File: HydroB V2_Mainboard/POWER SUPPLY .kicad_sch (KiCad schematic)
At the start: 6 parts, among them U2 TPS7A2633DRVR

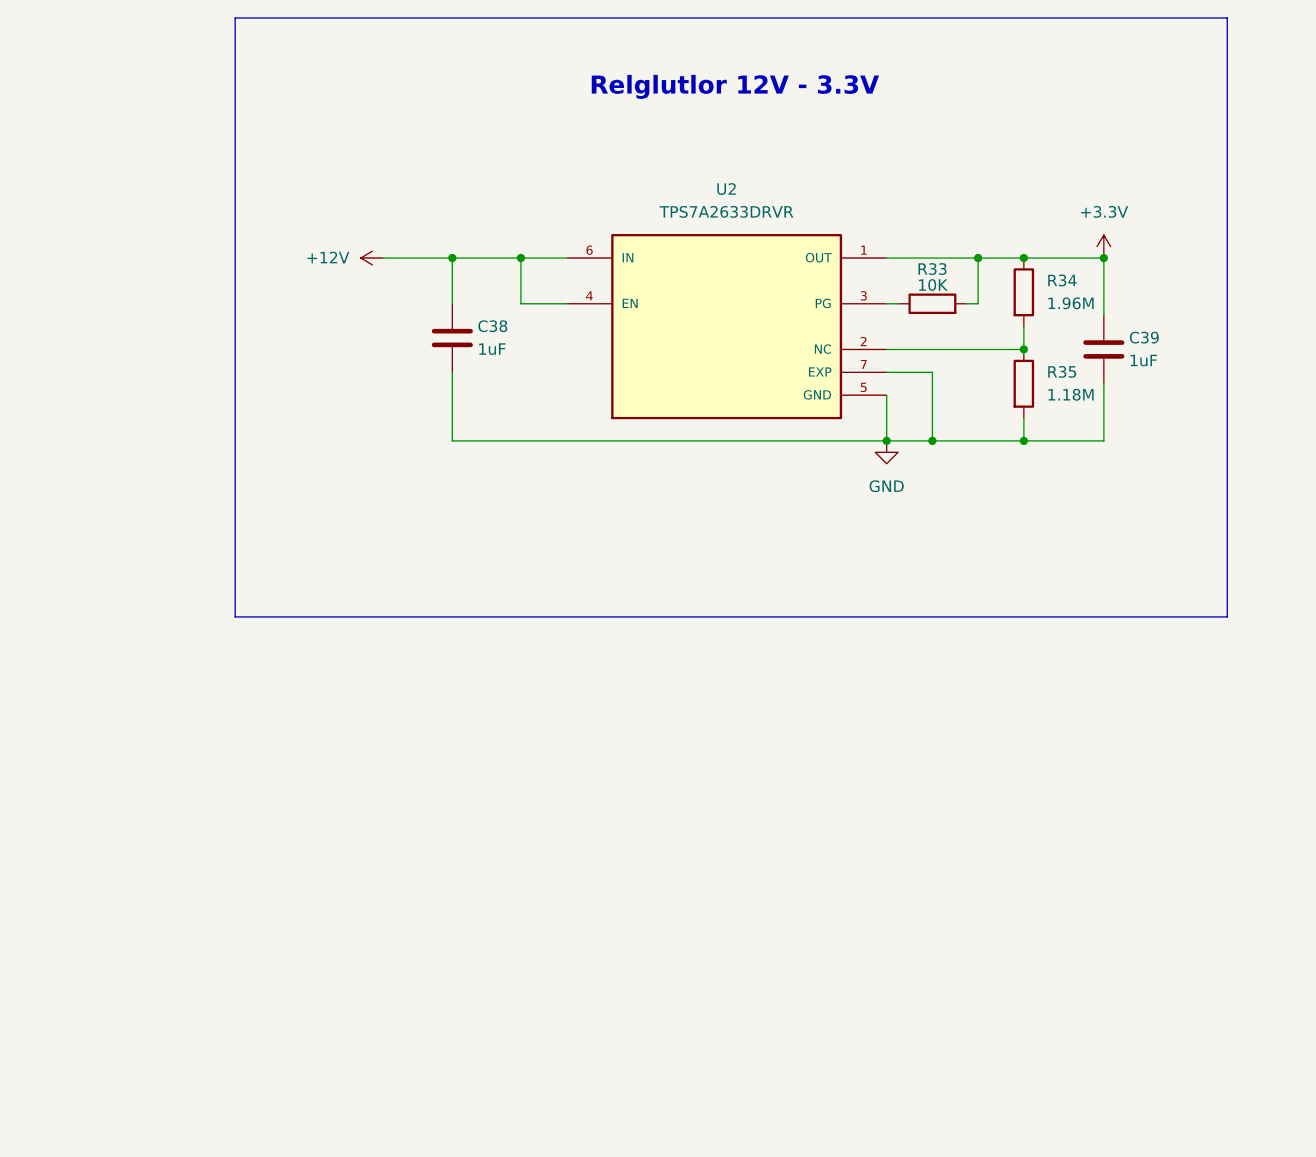
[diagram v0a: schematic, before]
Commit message: Update LCD schematic
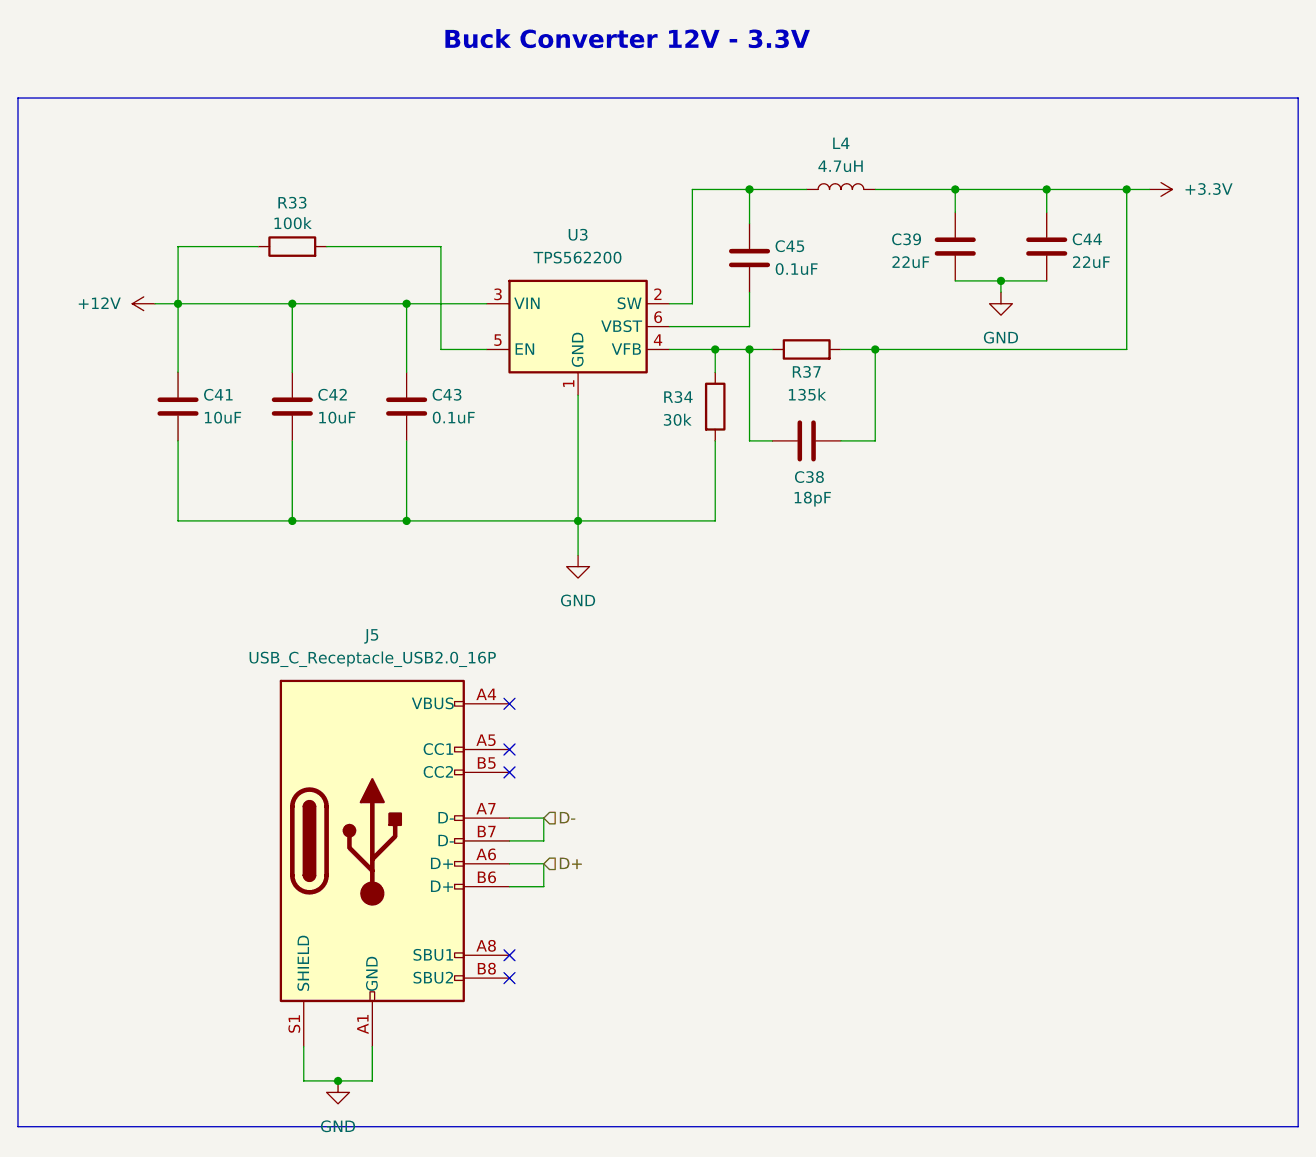
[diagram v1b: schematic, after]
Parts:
- removed R35: 1.18M, Resistor_SMD:R_0603_1608Metric, symbol Device:R
- removed U2: TPS7A2633DRVR, TPS7A2633DRVR:SON65P200X200X80-7N, symbol TPS7A2633DRVR:TPS7A2633DRVR
- added C41, C42: 10uF, Capacitor_SMD:C_0603_1608Metric, symbol Device:C
- added C43, C45: 0.1uF, Capacitor_SMD:C_0603_1608Metric, symbol Device:C
- added C44: 22uF, Capacitor_SMD:C_0603_1608Metric, symbol Device:C
- added J5: USB_C_Receptacle_USB2.0_16P, symbol Connector:USB_C_Receptacle_USB2.0_16P
- added L4: 4.7uH, symbol Device:L
- added R37: 135k, Resistor_SMD:R_0603_1608Metric, symbol Device:R
- added U3: TPS562200, Package_TO_SOT_SMD:SOT-23-6, symbol Regulator_Switching:TPS562200
- C38: value 1uF -> 18pF
- C39: value 1uF -> 22uF
- R33: value 10K -> 100k
- R34: value 1.96M -> 30k
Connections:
- net +12V: now also R33.1, C41.1, C42.1, C43.1, U3.3 (VIN); no longer C38.1
- net +3.3V: now also C38.2, C44.1, L4.2, R37.2; no longer R33.2, R34.1
- net GND: now also R34.2, C41.2, C42.2, C43.2, C44.2, J5.A1 (GND), J5.A12 (GND), J5.B1 (GND), J5.B12 (GND), J5.S1 (SHIELD), U3.1 (GND); no longer C38.2
- new net: C45.1, L4.1, U3.2 (SW)
- new net: C45.2, U3.6 (VBST)
- new net: C38.1, R34.1, R37.1, U3.4 (VFB)
- new net: R33.2, U3.5 (EN)
- new net: J5.A4 (VBUS), J5.A9 (VBUS), J5.B4 (VBUS), J5.B9 (VBUS)
- new net D+: J5.A6 (D+), J5.B6 (D+)
- new net D-: J5.A7 (D-), J5.B7 (D-)
- no-connect marks 0 -> 5
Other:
- note added: "Buck Converter 12V - 3.3V"
- note removed: "Relglutlor 12V - 3.3V"
- moved on the sheet: C38, C39, R33, R34

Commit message: Schematic mainboard update
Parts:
- added C10: 0.1uF, Capacitor_SMD:C_0603_1608Metric, symbol Device:C_Small
- added C11, C12: 22uF, Capacitor_SMD:C_0603_1608Metric, symbol Device:C_Small
- added C7: 10uF, Capacitor_SMD:CP_Elec_4x3, symbol Device:C
- added C8: 0.1uF, Capacitor_SMD:C_0603_1608Metric, symbol Device:C
- added C9: 75pF, Capacitor_SMD:C_0603_1608Metric, symbol Device:C_Small
- added J1: Conn_01x02_Pin, Connector_Phoenix_MC:PhoenixContact_MCV_1,5_2-G-3.81_1x02_P3.81mm_Vertical, symbol Connector:Conn_01x02_Pin
- added L1: 15uH, Inductor_SMD:L_Vishay_IHLP-2020, symbol Device:L
- added PS1: HLK-20M12, Converter_ACDC:Converter_ACDC_Hi-Link_HLK-20Mxx, symbol Converter_ACDC:HLK-20M12
- added R12: 100K, Resistor_SMD:R_0603_1608Metric, symbol Device:R
- added R13: 13.3K, Resistor_SMD:R_0603_1608Metric, symbol Device:R
- added R14: 49.9, Resistor_SMD:R_0603_1608Metric, symbol Device:R
- added R5: 1k, Resistor_SMD:R_0402_1005Metric, symbol Device:R
- added U4: TPS54202DDC, Package_TO_SOT_SMD:SOT-23-6, symbol Regulator_Switching:TPS54202DDC
- C41: footprint Capacitor_SMD:C_0603_1608Metric -> Capacitor_SMD:CP_Elec_4x3
- J5: footprint (none) -> Connector_USB:USB_C_Receptacle_G-Switch_GT-USB-7010ASV
- L4: footprint (none) -> Inductor_SMD:L_Bourns_SRP5030T
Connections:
- net +12V: now also C7.1, C8.1, PS1.4 (+Vout), U4.3 (VIN)
- net GND: now also C11.2, C12.2, C7.2, C8.2, PS1.3 (-Vout), R13.2, U4.1 (GND)
- net +5V: now reaches J5.A4 (VBUS), J5.A9 (VBUS), J5.B4 (VBUS), J5.B9 (VBUS)
- net +5V: now also C11.1, C12.1, L1.2, R14.2
- net A5: now reaches J5.A5 (CC1)
- new net: C9.2, R12.2, R13.1, U4.4 (FB)
- new net: C9.1, R12.1, R14.1
- new net: R5.1, U4.5 (EN)
- new net: C10.2, L1.1, U4.2 (SW)
- new net: C10.1, U4.6 (BOOT)
- new net En: R5.2
- new net L: J1.2 (Pin_2), PS1.1 (AC/L)
- new net N: J1.1 (Pin_1), PS1.2 (AC/N)
- no-connect marks 5 -> 3
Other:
- note added: "AC/DC input 220V-12V"
- note added: "Buck Converter 12V - 5V - 3.3V"
- note added: "Type C"
- note removed: "Buck Converter 12V - 3.3V"
- moved on the sheet: C38, C39, C41, C42, C43, C44, C45, J5, L4, R33, R34, R37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

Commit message: Mainboard schematic update
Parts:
- removed C10: 0.1uF, Capacitor_SMD:C_0603_1608Metric, symbol Device:C_Small
- removed C11, C12: 22uF, Capacitor_SMD:C_0603_1608Metric, symbol Device:C_Small
- removed C38: 18pF, Capacitor_SMD:C_0603_1608Metric, symbol Device:C
- removed C39, C44: 22uF, Capacitor_SMD:C_0603_1608Metric, symbol Device:C
- removed C41: 10uF, Capacitor_SMD:CP_Elec_4x3, symbol Device:C
- removed C42: 10uF, Capacitor_SMD:C_0603_1608Metric, symbol Device:C
- removed C43, C45: 0.1uF, Capacitor_SMD:C_0603_1608Metric, symbol Device:C
- removed C9: 75pF, Capacitor_SMD:C_0603_1608Metric, symbol Device:C_Small
- removed J1: Conn_01x02_Pin, Connector_Phoenix_MC:PhoenixContact_MCV_1,5_2-G-3.81_1x02_P3.81mm_Vertical, symbol Connector:Conn_01x02_Pin
- removed L4: 4.7uH, Inductor_SMD:L_Bourns_SRP5030T, symbol Device:L
- removed PS1: HLK-20M12, Converter_ACDC:Converter_ACDC_Hi-Link_HLK-20Mxx, symbol Converter_ACDC:HLK-20M12
- removed R33: 100k, Resistor_SMD:R_0603_1608Metric, symbol Device:R
- removed R34: 30k, Resistor_SMD:R_0603_1608Metric, symbol Device:R
- removed R37: 135k, Resistor_SMD:R_0603_1608Metric, symbol Device:R
- removed U3: TPS562200, Package_TO_SOT_SMD:SOT-23-6, symbol Regulator_Switching:TPS562200
- removed U4: TPS54202DDC, Package_TO_SOT_SMD:SOT-23-6, symbol Regulator_Switching:TPS54202DDC
- added C10, C11, C12, C13: 22uF, Capacitor_SMD:C_0805_2012Metric, symbol Device:C
- added C14, C15: 1uF, Capacitor_SMD:C_0805_2012Metric, symbol Device:C
- added C4: 10uF, Capacitor_SMD:CP_Elec_4x3, symbol Device:C
- added C6: 220nF, Capacitor_SMD:C_0805_2012Metric, symbol Device:C
- added C9: c, Capacitor_SMD:C_0805_2012Metric, symbol Device:C
- added D2: LED, LED_SMD:LED_0603_1608Metric_Pad1.05x0.95mm_HandSolder, symbol Device:LED
- added J6: 12V, DC Conn:DC conn, symbol Connector:Screw_Terminal_01x02
- added J7: Conn_01x02_Pin, Connector_PinHeader_2.00mm:PinHeader_1x02_P2.00mm_Vertical, symbol Connector:Conn_01x02_Pin
- added R15: 1.96M, Resistor_SMD:R_0402_1005Metric, symbol Device:R
- added R16: 1.18M, Resistor_SMD:R_0402_1005Metric, symbol Device:R
- added R17: 1k, Resistor_SMD:R_0603_1608Metric, symbol Device:R
- added U3: LMR33620ADDA, Package_SO:Texas_HSOP-8-1EP_3.9x4.9mm_P1.27mm_ThermalVias, symbol Regulator_Switching:LMR33620ADDA
- added U4: TPS7A2633DRVR, TPS7A2633DRVR:SON65P200X200X80-7N, symbol TPS7A2633DRVR:TPS7A2633DRVR
- C7: value 10uF -> 1uF; footprint Capacitor_SMD:CP_Elec_4x3 -> Capacitor_SMD:C_0805_2012Metric
- C8: value 0.1uF -> 100NF
- L1: value 15uH -> 10uH; footprint Inductor_SMD:L_Vishay_IHLP-2020 -> Inductor_SMD:L_Bourns_SRP5030T
- R12: value 100K -> 100k
- R13: value 13.3K -> 43.2k
- R14: value 49.9 -> 10K
- R5: value 1k -> 100k; footprint Resistor_SMD:R_0402_1005Metric -> Resistor_SMD:R_0603_1608Metric
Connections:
- net +12V: now also C4.1, C6.1, J6.1 (Pin_1), U3.2 (VIN), U3.3 (EN); no longer C7.1, C8.1
- net +3.3V: now also R14.2, C15.1, D2.2 (A), J7.1 (Pin_1), R15.1, U4.1 (OUT)
- net +5V: now also C14.1, U4.4 (EN), U4.6 (IN); no longer L1.2, R14.2
- net GND: now also R13.1, C10.2, C11.2, C12.2, C13.2, C14.2, C15.2, C4.2, C6.2, J6.2 (Pin_2), R16.2, R17.2, U3.1 (GND), U3.9 (GND), U4.5 (GND), U4.7 (EXP); no longer C8.2, R13.2
- net SW_OUT: now reaches R12.2
- net SW_OUT: now also L1.2, C10.1, C11.1, C12.1, C13.1, C9.1, J7.2 (Pin_2); no longer R13.1
- net at R12.1: now also R13.2, C9.2, U3.5 (FB); no longer R14.1
- net PG: now reaches R5.1
- net PG: now also U3.4 (PG)
- net SW: now reaches L1.1
- net SW: now also C8.2, U3.8 (SW)
- net A5: no longer names the net of J5.A5 (CC1)
- net En: no longer names the net of R5.2
- net En: now also C7.1, U3.6 (VCC)
- new net: R15.2, R16.1, U4.2 (NC)
- new net: D2.1 (K), R17.1
- new net: R14.1, U4.3 (PG)
- new net: C8.1, U3.7 (BOOT)
- no-connect marks 3 -> 5
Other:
- note added: "Buck Converter 12V - 3.3V 2A"
- note removed: "AC/DC input 220V-12V"
- note removed: "Buck Converter 12V - 5V - 3.3V"
- moved on the sheet: J5

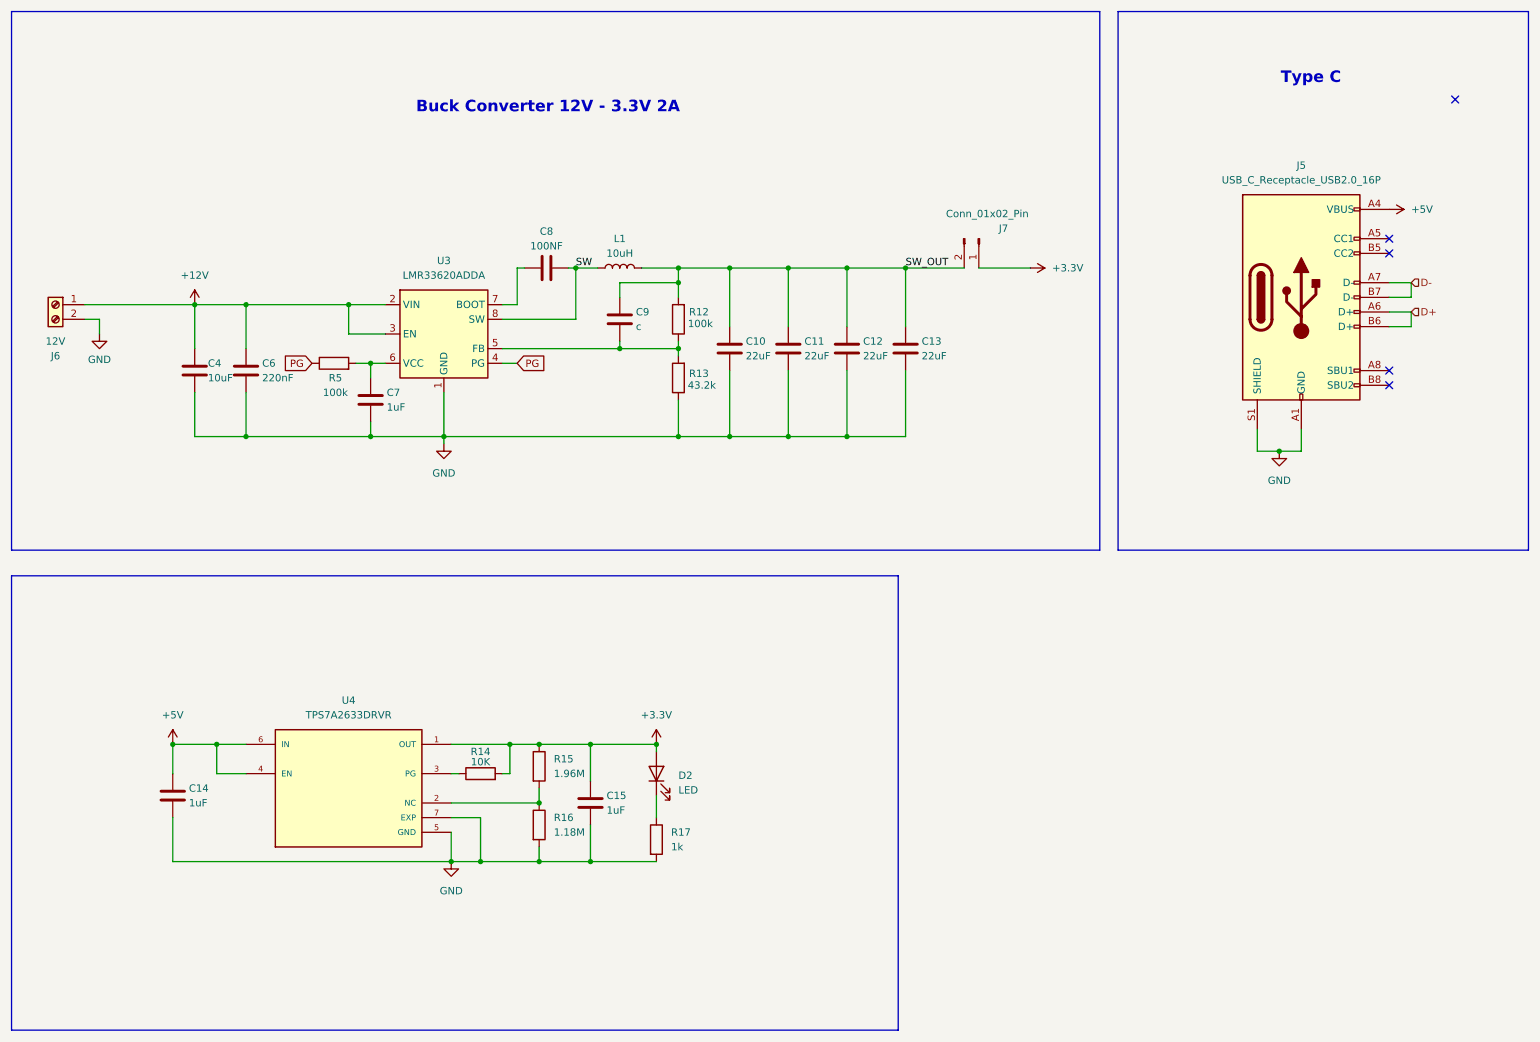
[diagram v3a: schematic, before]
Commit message: main PCB board placement
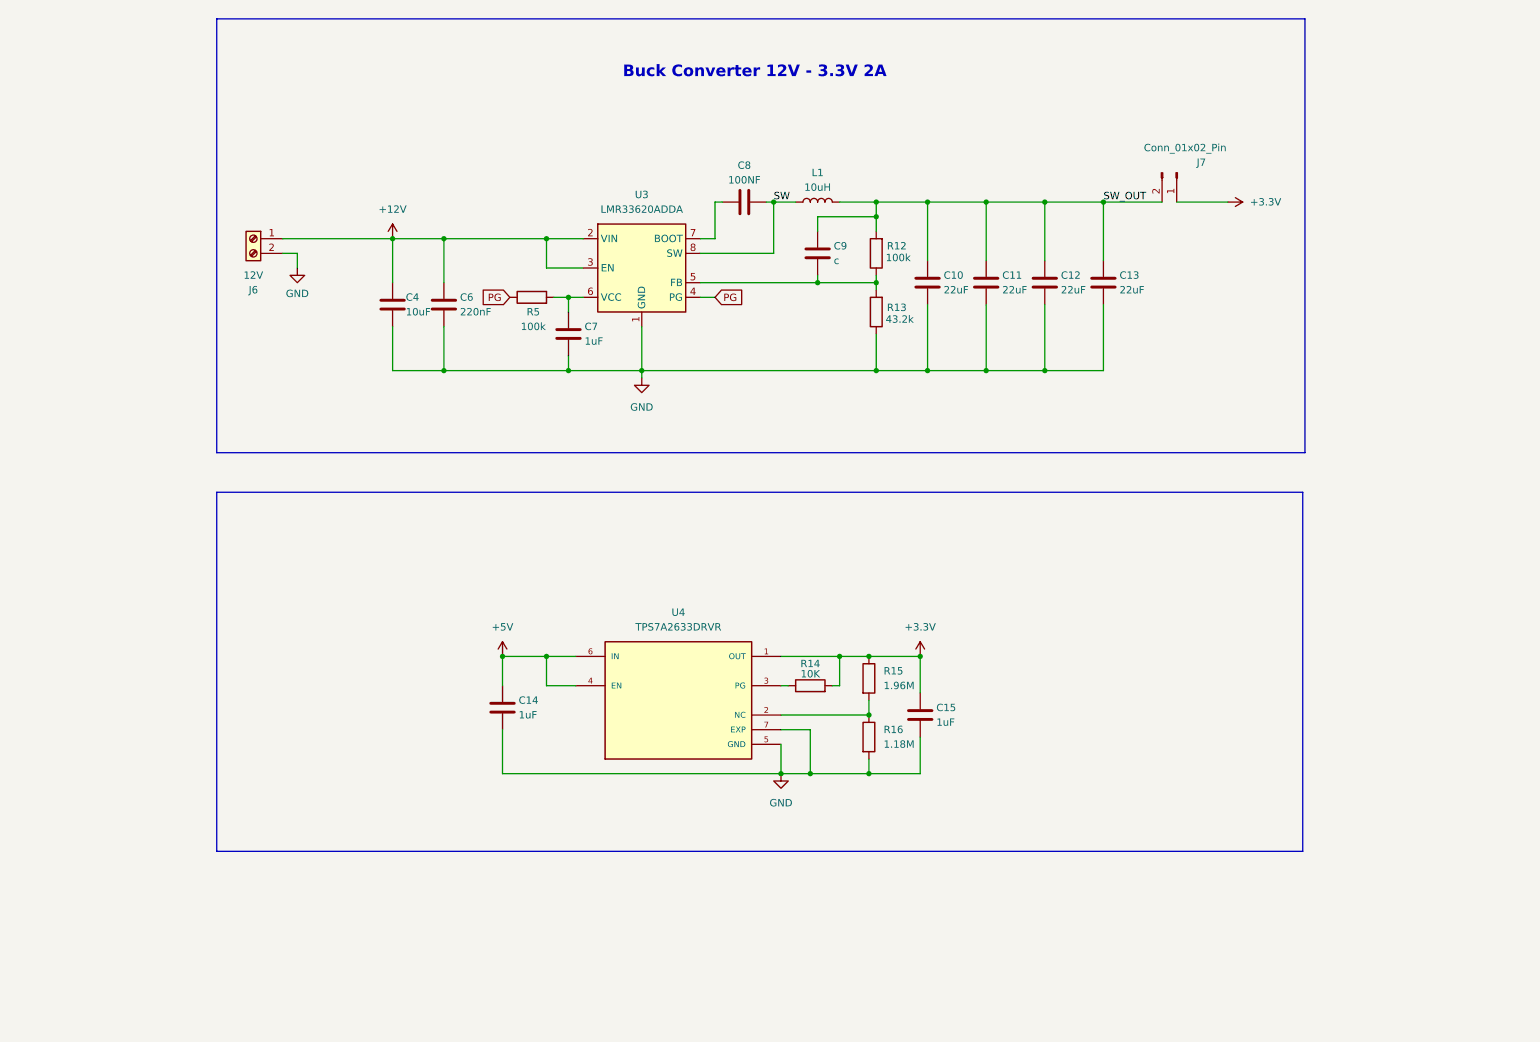
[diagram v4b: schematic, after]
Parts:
- removed D2: LED, LED_SMD:LED_0603_1608Metric_Pad1.05x0.95mm_HandSolder, symbol Device:LED
- removed J5: USB_C_Receptacle_USB2.0_16P, Connector_USB:USB_C_Receptacle_G-Switch_GT-USB-7010ASV, symbol Connector:USB_C_Receptacle_USB2.0_16P
- removed R17: 1k, Resistor_SMD:R_0603_1608Metric, symbol Device:R
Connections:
- no-connect marks 5 -> 0
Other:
- note removed: "Type C"
- moved on the sheet: C10, C11, C12, C13, C14, C15, C4, C6, C7, C8, C9, J6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

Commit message: PCB placement and ERC
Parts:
- removed U4: TPS7A2633DRVR, TPS7A2633DRVR:SON65P200X200X80-7N, symbol TPS7A2633DRVR:TPS7A2633DRVR
- added U5: TPS7A2633DRVR, TPS7A2633DRVR:SON65P200X200X80-7N, symbol TPS7A2633DRVR:TPS7A2633DRVR
- L1: value 10uH -> 2.2uH
- R13: value 43.2k -> 24.9k
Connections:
- net +3.3V: now also U5.1 (OUT); no longer J7.1 (Pin_1)
- net GND: now also U5.5 (GND), U5.7 (EXP)
- net at R15.2, R16.1: now also U5.2 (NC)
- net at R14.1: now also U5.3 (PG)
- net +5V renamed VBUS
- net VBUS: now also J7.1 (Pin_1), U5.4 (EN), U5.6 (IN)
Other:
- note added: "Buck Converter 12V - 5V - 3.3V"
- note removed: "Buck Converter 12V - 3.3V 2A"
- company: (none) -> Power Supply
- title: (none) -> Prak Chilifong
- moved on the sheet: C14, C15, R14, R15, R16
